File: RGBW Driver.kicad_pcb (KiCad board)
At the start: 2 copper layers, 22.1 x 59.5 mm, 25 parts, among them J1 LED, J2 LED, J3 LED, J4 LED, J5 Power, U1 PT4115, U2 PT4115, U3 PT4115, U4 PT4115

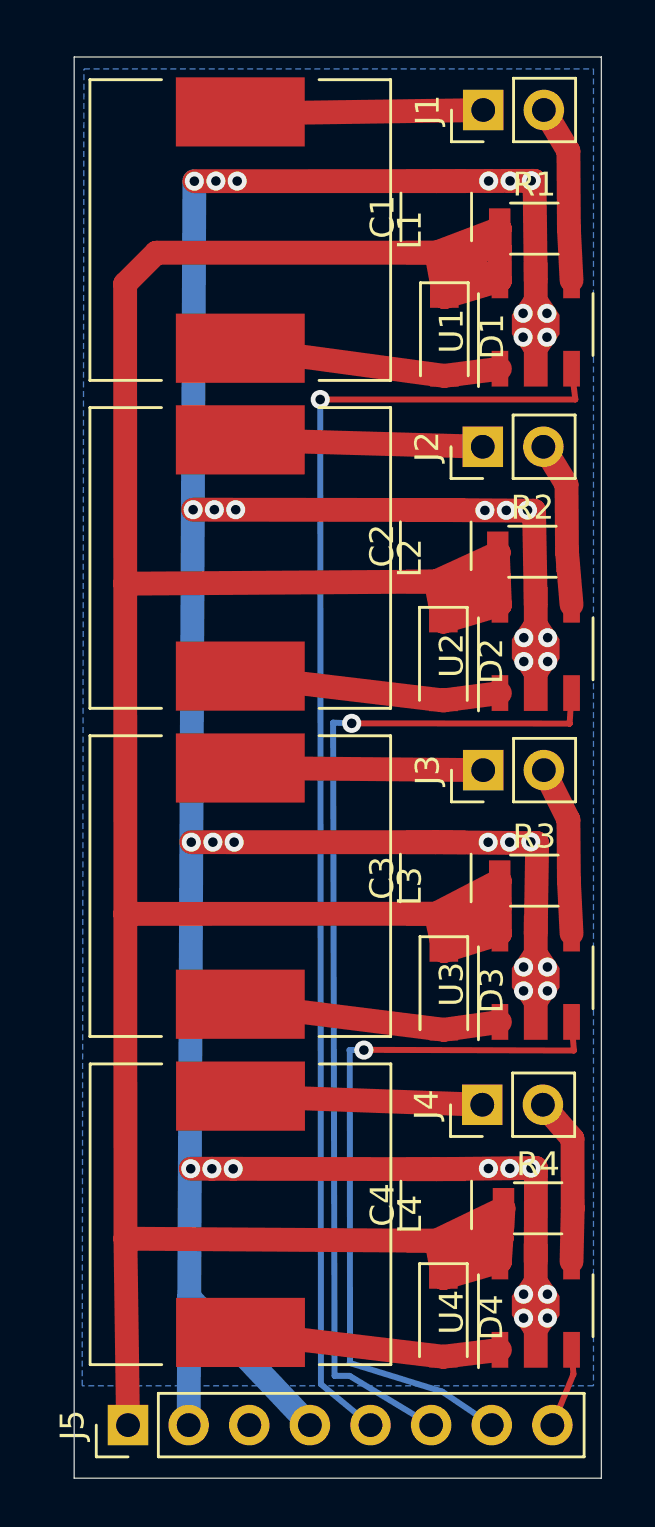
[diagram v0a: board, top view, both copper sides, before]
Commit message: Place-replicate the layout
also replaced some trackign with filled zones.
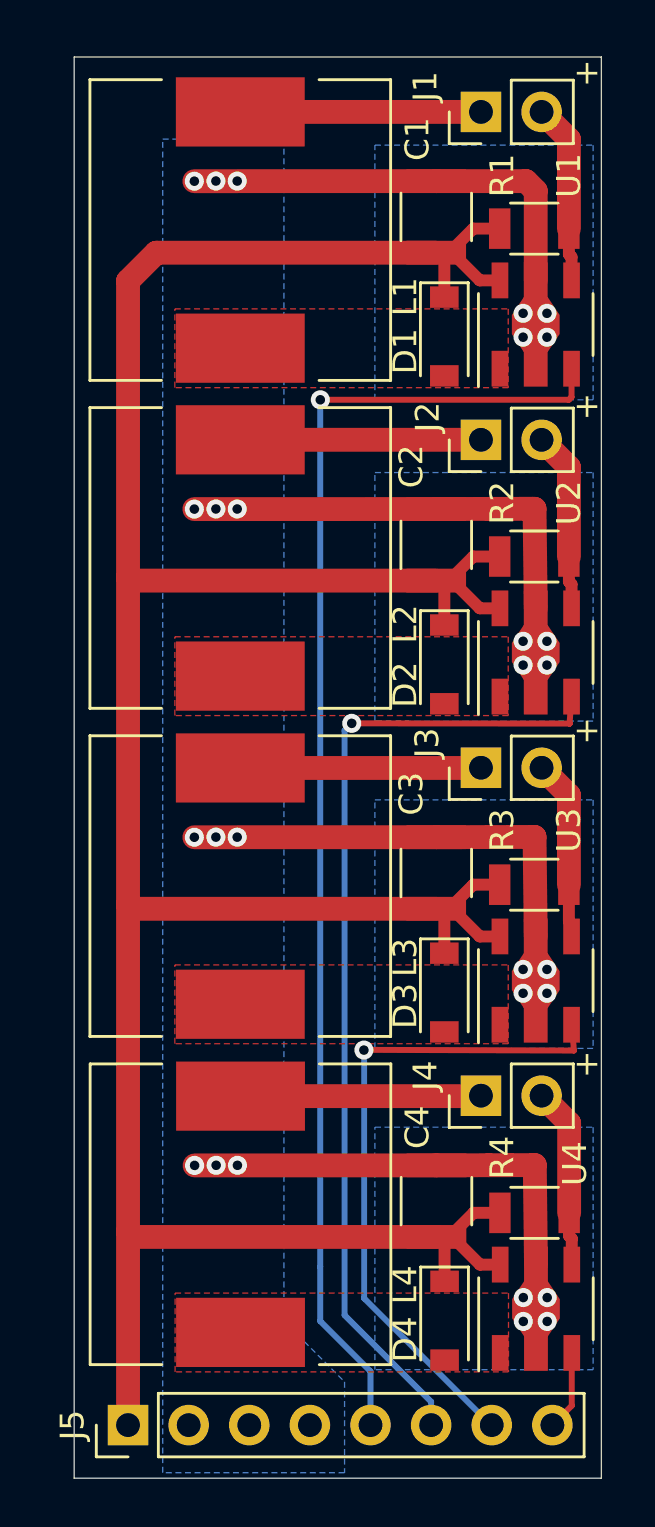
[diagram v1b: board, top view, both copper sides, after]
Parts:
- moved J4 0.38 mm to (88.3, 64.2)
- moved J2 0.30 mm to (88.3, 36.7)
- moved R4 0.24 mm to (90.5, 69.1)
- moved R2 0.22 mm to (90.5, 41.6)
- moved C3 0.21 mm to (86.4, 54.9)
- moved R3 0.17 mm to (90.5, 55.4)
- moved C4 0.16 mm to (86.4, 68.6)
- moved U2 0.15 mm to (90.6, 45.6)
- moved D4 0.15 mm to (86.7, 73.6)
- moved D2 0.15 mm to (86.7, 46.1)
- moved J3 0.14 mm to (88.3, 50.5)
- moved U4 0.13 mm to (90.6, 73.1)
- moved J1 0.12 mm to (88.3, 23.0)
- moved U3 0.12 mm to (90.6, 59.4)
- moved D3 0.09 mm to (86.7, 59.9)
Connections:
- net /Dim1 renamed /Sheet5F4096CF/Dim
- net /Dim2 renamed /sheet5F46240A/Dim
- net /Dim3 renamed /sheet5F46272E/Dim
- net /Dim4 renamed /sheet5F462A40/Dim
- net /Gnd renamed /Sheet5F4096CF/GND
- net /LED1+ renamed /Sheet5F4096CF/LED+
- net /LED1- renamed /Sheet5F4096CF/LED-
- net /LED2+ renamed /sheet5F46240A/LED+
- net /LED2- renamed /sheet5F46240A/LED-
- net /LED3+ renamed /sheet5F46272E/LED+
- net /LED3- renamed /sheet5F46272E/LED-
- net /LED4+ renamed /sheet5F462A40/LED+
- net /LED4- renamed /sheet5F462A40/LED-
- net /SW1 renamed /Sheet5F4096CF/SW1
- net /SW2 renamed /sheet5F46240A/SW1
- net /SW3 renamed /sheet5F46272E/SW1
- net /SW4 renamed /sheet5F462A40/SW1
- net /Vin renamed /Sheet5F4096CF/Vin
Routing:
- net /Sheet5F4096CF/GND: track 143.9 -> 88.3 mm, vias 40 -> 28
- net /Sheet5F4096CF/Vin: track 172.2 -> 133.2 mm
- net /Sheet5F4096CF/SW1: track 11.0 -> 0.00 mm
- net /sheet5F46272E/SW1: track 11.0 -> 0.00 mm
- net /sheet5F46240A/SW1: track 11.0 -> 0.00 mm
- net /sheet5F462A40/SW1: track 10.9 -> 0.00 mm
- net /sheet5F46272E/Dim: track 30.3 -> 27.9 mm
- net /sheet5F46240A/Dim: track 43.2 -> 41.5 mm
- net /sheet5F46240A/LED+: track 6.90 -> 7.58 mm
- net /sheet5F462A40/LED+: track 7.03 -> 7.60 mm
- added copper zone on F.Cu, net /Sheet5F4096CF/SW1
- added copper zone on F.Cu, net /sheet5F46240A/SW1
- added copper zone on F.Cu, net /sheet5F46272E/SW1
- added copper zone on F.Cu, net /sheet5F462A40/SW1
- removed copper zone on F.Cu, net /Sheet5F4096CF/Vin
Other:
- board text added: "+"
